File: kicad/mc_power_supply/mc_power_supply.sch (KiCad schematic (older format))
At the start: 20 parts

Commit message: Приступил к разработке блока питания ver.3 для измерительного микрофофона.
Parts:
- added C1, C2: 1 мк 275В, symbol LFcapitors:CAPITORS
- added LL1: B82731T2301A020, symbol LFtransformator:CHOKES_PL
- added R1: 500 к, symbol LFresistor:RESISTOR
- added RU1: B72210S0271K101, symbol LFresistor:VARISTOR
- added XP2: L-KLS8-01128-PC-250-0.8, ~, symbol LFconnectors:connector_1pin_gost
- C3: renamed from C1; value 470 мк 35 В -> 4700 мк 35 В; footprint (none) -> IWcomponents:CAPACITOR_10_D22
- C4: renamed from C2; value 47 мк 25 В -> 470 мк 35 В; footprint (none) -> IWcomponents:CAPACITOR_5.08_D13
- C5: renamed from C3; footprint (none) -> IWsmd_case:SMD0805
- R2: renamed from R1; footprint (none) -> IWsmd_case:SMD0805
- VD1, VD2, VD3, VD4, VD5: value MBRS1100T3G -> VS-10MQ100NTRPBF
- VD6: renamed from VD5; value GNL-3014PGC -> GNL-3014BC
- XP1: renamed from XS1; value DG126-5.0-02P-14 -> L-KLS8-01128-PC-250-0.8; symbol LFconnectors:connector_2pin_gost -> LFconnectors:connector_1pin_gost
- XP3: renamed from XP1; footprint ~ -> IWconnectors:WF-2
- XS1: renamed from XS3; value WF-3 -> Neutrik NC3FD-L1
- XS2: renamed from XS4; value WF-2 -> BNC-BJ
- renumbered R2 to R3, R3 to R4, XS2 to XS3
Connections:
- net at TV1.1: now also C2.1, LL1.3; no longer FU1.2
- net at TV1.5: now also C2.2, LL1.4; no longer XP1.2
- new net: C1.1, FU1.2, LL1.2, R1.2, RU1.1
- new net: C1.2, LL1.1, R1.1, RU1.2, XP2.1
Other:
- note added: "* Источник питания предназначен для\n питания микрофонного усилителя.\n Диапазон выходного напряжения\n от 9В до 15В при токе 0.5А"
- note removed: "* Источник питания выдаёт напряжение\n для питания микрофонного усилителя\n в диапазоне от 9В до 15В при токе 0.5А"
- moved on the sheet: C3, C4, C5, DA1, FU1, R2, R3, R4, TV1, VD1, VD2, VD3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

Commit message: Приступил к расположению компонентов на плате mc_power_supply_ver3.
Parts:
- C1, C2: footprint (none) -> IWcomponents:CAPACITOR_B32923_26.5x11
- C4: footprint IWcomponents:CAPACITOR_5.08_D13 -> IWcomponents:CAPACITOR_5.08_D10
- DA1: value LM317KTTR -> LM317D2T-TR; footprint ~ -> Package_TO:TO-263-3_TabPin2
- FU1: footprint ~ -> IWcomponents:FU_PTF15B
- LL1: footprint (none) -> IWtransformator:EMI_EPCOS_B82731T
- R1: footprint (none) -> IWsmd_case:SMD2512
- R3: footprint (none) -> IWsmd_case:BOURNS_3224W
- RU1: footprint (none) -> IWcomponents:RU_EPCOS_B72210S0271K101_12х5
- TV1: value ТПГ-112 (12В) -> ТПГ-112-12; footprint (none) -> IWtransformator:TPG112-12; symbol LFtransformator:BVEI_302_2020 -> LFtransformator:TPG-112-12
- VD1, VD2, VD3, VD4, VD5: footprint (none) -> IWcomponents:SMA
- XP1, XP2: footprint ~ -> IWconnectors:TERMINAL_KLS8-01128_6.3mm
- XS1, XS2, XS3: footprint ~ -> (none)
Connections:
- net at C2.1, LL1.3: now also TV1.5; no longer TV1.1
- net at C2.2, LL1.4: now also TV1.1; no longer TV1.5
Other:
- moved on the sheet: C1, C2, FU1, LL1, R1, RU1, XP1, XP2
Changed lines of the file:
@@
 P 8650 3750
 F 0 "DA1" H 8900 3900 60  0000 C CNN
-F 1 "LM317KTTR" H 8900 3800 60  0000 C CNN
-F 2 "~" H 8650 3750 60  0000 C CNN
+F 1 "LM317D2T-TR" H 8900 3800 60  0000 C CNN
+F 2 "Package_TO:TO-263-3_TabPin2" H 8650 3750 60  0001 C CNN
 F 3 "~" H 8650 3750 60  0000 C CNN
 	1    8650 3750
@@
 $EndComp
 $Comp
-L LFtransformator:BVEI_302_2020 TV1
+L LFtransformator:TPG-112-12 TV1
 U 1 1 55462143
 P 5850 4300
-F 0 "TV1" H 6050 4500 60  0000 C CNN
-F 1 "ТПГ-112 (12В)" H 6050 4400 60  0000 C CNN
-F 2 "" H 5850 4300 60  0001 C CNN
+F 0 "TV1" H 6050 4650 60  0000 C CNN
+F 1 "ТПГ-112-12" H 6050 4500 60  0000 C CNN
+F 2 "IWtransformator:TPG112-12" H 5850 4300 60  0001 C CNN
 F 3 "" H 5850 4300 60  0000 C CNN
 	1    5850 4300
@@
 L LFcomponents:PROTECTOR FU1
 U 1 1 5546217A
-P 3100 4200
-F 0 "FU1" H 3200 4450 60  0000 C CNN
-F 1 "0.25 A" H 3200 4350 60  0000 C CNN
-F 2 "~" H 3100 4200 60  0000 C CNN
-F 3 "~" H 3100 4200 60  0000 C CNN
-	1    3100 4200
+P 3250 4200
+F 0 "FU1" H 3350 4450 60  0000 C CNN
+F 1 "0.25 A" H 3350 4350 60  0000 C CNN
+F 2 "IWcomponents:FU_PTF15B" H 3250 4200 60  0001 C CNN
+F 3 "~" H 3250 4200 60  0000 C CNN
+	1    3250 4200
 	1    0    0    -1
 $EndComp
@@
 L LFconnectors:connector_1pin_gost XP1
 U 1 1 554621C8
-P 2750 4200
-F 0 "XP1" H 3100 4500 50  0000 L BNN
-F 1 "L-KLS8-01128-PC-250-0.8" H 2600 4400 50  0000 L BNN
-F 2 "~" H 3200 4350 50  0001 C CNN
-F 3 "" H 2750 4200 60  0000 C CNN
-	1    2750 4200
+P 2900 4200
+F 0 "XP1" H 3250 4500 50  0000 L BNN
+F 1 "L-KLS8-01128-PC-250-0.8" H 2750 4400 50  0000 L BNN
+F 2 "IWconnectors:TERMINAL_KLS8-01128_6.3mm" H 3350 4350 50  0001 C CNN
+F 3 "" H 2900 4200 60  0000 C CNN
+	1    2900 4200
 	-1   0    0    -1
 $EndComp
 Wire Wire Line
-	2750 4200 3100 4200
+	2900 4200 3250 4200
 $Comp
 L LFdiod:SHOTTKY_DIODE VD1
@@
 F 0 "VD1" H 7100 4200 71  0000 C CNN
 F 1 "VS-10MQ100NTRPBF" H 7250 4050 71  0000 C CNN
-F 2 "" H 6750 4300 60  0001 C CNN
+F 2 "IWcomponents:SMA" H 6750 4300 60  0001 C CNN
 F 3 "" H 6750 4300 60  0000 C CNN
 	1    6750 4300
@@
 F 0 "VD4" H 7900 4750 71  0000 C CNN
 F 1 "VS-10MQ100NTRPBF" H 7800 4650 71  0000 C CNN
-F 2 "" H 7750 4300 60  0001 C CNN
+F 2 "IWcomponents:SMA" H 7750 4300 60  0001 C CNN
 F 3 "" H 7750 4300 60  0000 C CNN
 	1    7750 4300
@@
 F 0 "VD2" H 7200 4400 71  0000 C CNN
 F 1 "VS-10MQ100NTRPBF" H 7350 4250 71  0000 C CNN
-F 2 "" H 7050 4750 60  0001 C CNN
+F 2 "IWcomponents:SMA" H 7050 4750 60  0001 C CNN
 F 3 "" H 7050 4750 60  0000 C CNN
 	1    7050 4750
@@
 F 0 "VD3" H 7600 4400 71  0000 C CNN
 F 1 "VS-10MQ100NTRPBF" H 7950 4250 71  0000 C CNN
-F 2 "" H 7450 4750 60  0001 C CNN
+F 2 "IWcomponents:SMA" H 7450 4750 60  0001 C CNN
 F 3 "" H 7450 4750 60  0000 C CNN
 	1    7450 4750
@@
 F 0 "R3" V 9600 4450 71  0000 C CNN
 F 1 "5 к" V 9700 4450 71  0000 C CNN
-F 2 "" H 9500 4650 60  0001 C CNN
+F 2 "IWsmd_case:BOURNS_3224W" H 9500 4650 60  0001 C CNN
 F 3 "" H 9500 4650 60  0000 C CNN
 	1    9500 4650
@@
 F 0 "XS1" H 12450 4900 50  0000 L BNN
 F 1 "Neutrik NC3FD-L1" H 12250 4800 50  0000 L BNN
-F 2 "~" H 12650 4750 50  0001 C CNN
+F 2 "" H 12650 4750 50  0001 C CNN
 F 3 "" H 12200 4600 60  0000 C CNN
 	1    12200 4600
@@
 F 0 "XS2" H 12500 5850 50  0000 L BNN
 F 1 "BNC-BJ " H 12400 5750 50  0000 L BNN
-F 2 "~" H 12700 5700 50  0001 C CNN
+F 2 "" H 12700 5700 50  0001 C CNN
 F 3 "" H 12250 5550 60  0000 C CNN
 	1    12250 5550
@@
 F 0 "VD5" H 9250 3700 71  0000 C CNN
 F 1 "VS-10MQ100NTRPBF" H 9250 3600 71  0000 C CNN
-F 2 "" H 9100 3450 60  0001 C CNN
+F 2 "IWcomponents:SMA" H 9100 3450 60  0001 C CNN
 F 3 "" H 9100 3450 60  0000 C CNN
 	1    9100 3450
@@
 Text Notes 12635 4640 0    50   ~ 0
 GND
-Text Notes 2020 4240 0    50   ~ 0
+Text Notes 2170 4240 0    50   ~ 0
 220В 50Гц
 Text Notes 2250 7050 0    60   ~ 0
@@
 F 0 "C4" H 10450 4550 71  0000 C CNN
 F 1 "470 мк 35 В" H 10450 4450 71  0000 C CNN
-F 2 "IWcomponents:CAPACITOR_5.08_D13" H 10250 4250 60  0001 C CNN
+F 2 "IWcomponents:CAPACITOR_5.08_D10" H 10250 4250 60  0001 C CNN
 F 3 "" H 10250 4250 60  0000 C CNN
 	1    10250 4250
@@
 F 0 "XS3" H 13300 4300 50  0000 L BNN
 F 1 "HU-2" H 13250 4200 50  0000 L BNN
-F 2 "~" H 13400 4150 50  0001 C CNN
+F 2 "" H 13400 4150 50  0001 C CNN
 F 3 "" H 12950 4000 60  0000 C CNN
 	1    12950 4000
@@
 L LFconnectors:connector_1pin_gost XP2
 U 1 1 60118508
-P 2750 4700
-F 0 "XP2" H 3100 5000 50  0000 L BNN
-F 1 "L-KLS8-01128-PC-250-0.8" H 2600 4900 50  0000 L BNN
-F 2 "~" H 3200 4850 50  0001 C CNN
-F 3 "" H 2750 4700 60  0000 C CNN
-	1    2750 4700
+P 2900 4700
+F 0 "XP2" H 3250 5000 50  0000 L BNN
+F 1 "L-KLS8-01128-PC-250-0.8" H 2750 4900 50  0000 L BNN
+F 2 "IWconnectors:TERMINAL_KLS8-01128_6.3mm" H 3350 4850 50  0001 C CNN
+F 3 "" H 2900 4700 60  0000 C CNN
+	1    2900 4700
 	-1   0    0    -1
 $EndComp
-Text Notes 2020 4740 0    50   ~ 0
+Text Notes 2170 4740 0    50   ~ 0
 220В 50Гц
 $Comp
 L LFcapitors:CAPITORS C1
 U 1 1 60135059
-P 4300 4350
-F 0 "C1" V 4750 4350 71  0000 C CNN
-F 1 "1 мк 275В" V 4900 4350 71  0000 C CNN
-F 2 "" H 4300 4350 60  0001 C CNN
-F 3 "" H 4300 4350 60  0000 C CNN
-	1    4300 4350
+P 4450 4350
+F 0 "C1" V 4900 4350 71  0000 C CNN
+F 1 "1 мк 275В" V 5050 4350 71  0000 C CNN
+F 2 "IWcomponents:CAPACITOR_B32923_26.5x11" H 4450 4350 60  0001 C CNN
+F 3 "" H 4450 4350 60  0000 C CNN
+	1    4450 4350
 	0    1    1    0
 $EndComp
 Wire Wire Line
-	3350 4200 3650 4200
-Wire Wire Line
-	4300 4600 4300 4700
-Wire Wire Line
-	2750 4700 3650 4700
+	3500 4200 3800 4200
+Wire Wire Line
+	4450 4600 4450 4700
+Wire Wire Line
+	2900 4700 3800 4700
 $Comp
 L LFtransformator:CHOKES_PL LL1
 U 1 1 60142715
-P 5200 4350
-F 0 "LL1" V 4953 4050 60  0000 C CNN
-F 1 "B82731T2301A020" V 5059 4050 60  0000 C CNN
-F 2 "" H 5200 4350 60  0001 C CNN
-F 3 "" H 5200 4350 60  0000 C CNN
-	1    5200 4350
+P 5350 4350
+F 0 "LL1" V 5103 4050 60  0000 C CNN
+F 1 "B82731T2301A020" V 5209 4050 60  0000 C CNN
+F 2 "IWtransformator:EMI_EPCOS_B82731T" H 5350 4350 60  0001 C CNN
+F 3 "" H 5350 4350 60  0000 C CNN
+	1    5350 4350
 	0    1    1    0
 $EndComp
 Wire Wire Line
-	4600 4350 4450 4350
-Wire Wire Line
-	4450 4200 4300 4200
-Connection ~ 4300 4200
-Wire Wire Line
-	4300 4700 4450 4700
-Wire Wire Line
-	4450 4700 4450 4550
-Wire Wire Line
-	4450 4550 4600 4550
-Connection ~ 4300 4700
-Wire Wire Line
-	5200 4350 5350 4350
-Wire Wire Line
-	5350 4350 5350 4200
-Wire Wire Line
-	5350 4200 5500 4200
-Wire Wire Line
-	5200 4550 5350 4550
-Wire Wire Line
-	5350 4550 5350 4700
-Wire Wire Line
-	5350 4700 5500 4700
+	4750 4350 4600 4350
+Wire Wire Line
+	4600 4200 4450 4200
+Connection ~ 4450 4200
+Wire Wire Line
+	4450 4700 4600 4700
+Wire Wire Line
+	4600 4700 4600 4550
+Wire Wire Line
+	4600 4550 4750 4550
+Connection ~ 4450 4700
+Wire Wire Line
+	5350 4350 5500 4350
+Wire Wire Line
+	5500 4350 5500 4200
+Wire Wire Line
+	5500 4200 5700 4200
+Wire Wire Line
+	5350 4550 5500 4550
+Wire Wire Line
+	5500 4550 5500 4700
+Wire Wire Line
+	5500 4700 5700 4700
 $Comp
 L LFresistor:RESISTOR R1
 U 1 1 6015F13E
-P 4000 4600
-F 0 "R1" V 4650 4600 71  0000 C CNN
-F 1 "500 к" V 4500 4600 71  0000 C CNN
-F 2 "" H 4000 4600 60  0001 C CNN
-F 3 "" H 4000 4600 60  0000 C CNN
-	1    4000 4600
+P 4150 4600
+F 0 "R1" V 4800 4600 71  0000 C CNN
+F 1 "500 к" V 4650 4600 71  0000 C CNN
+F 2 "IWsmd_case:SMD2512" H 4150 4600 60  0001 C CNN
+F 3 "" H 4150 4600 60  0000 C CNN
+	1    4150 4600
 	0    -1   -1   0
 $EndComp
-Connection ~ 4000 4200
-Wire Wire Line
-	4000 4200 4300 4200
-Wire Wire Line
-	4000 4600 4000 4700
-Connection ~ 4000 4700
-Wire Wire Line
-	4000 4700 4300 4700
+Connection ~ 4150 4200
+Wire Wire Line
+	4150 4200 4450 4200
+Wire Wire Line
+	4150 4600 4150 4700
+Connection ~ 4150 4700
+Wire Wire Line
+	4150 4700 4450 4700
 $Comp
 L LFresistor:VARISTOR RU1
 U 1 1 6016D315
-P 3650 4350
-F 0 "RU1" V 3900 3950 71  0000 L CNN
-F 1 "B72210S0271K101" V 4100 3550 71  0000 L CNN
-F 2 "" H 3650 4350 60  0001 C CNN
-F 3 "~" V 3856 4477 60  0000 L CNN
-	1    3650 4350
+P 3800 4350
+F 0 "RU1" V 4050 3950 71  0000 L CNN
+F 1 "B72210S0271K101" V 4250 3550 71  0000 L CNN
+F 2 "IWcomponents:RU_EPCOS_B72210S0271K101_12х5" H 3800 4350 60  0001 C CNN
+F 3 "~" V 4006 4477 60  0000 L CNN
+	1    3800 4350
 	0    1    1    0
 $EndComp
 Wire Wire Line
+	4600 4200 4600 4350
+Wire Wire Line
 	4450 4200 4450 4350
 Wire Wire Line
-	4300 4200 4300 4350
-Wire Wire Line
-	4000 4200 4000 4350
-Wire Wire Line
-	3650 4350 3650 4200
-Connection ~ 3650 4200
-Wire Wire Line
-	3650 4200 4000 4200
-Wire Wire Line
-	3650 4600 3650 4700
-Connection ~ 3650 4700
-Wire Wire Line
-	3650 4700 4000 4700
-Wire Wire Line
-	5500 4200 5500 4350
-Wire Wire Line
-	5500 4600 5500 4700
+	4150 4200 4150 4350
+Wire Wire Line
+	3800 4350 3800 4200
+Connection ~ 3800 4200
+Wire Wire Line
+	3800 4200 4150 4200
+Wire Wire Line
+	3800 4600 3800 4700
+Connection ~ 3800 4700
+Wire Wire Line
+	3800 4700 4150 4700
+Wire Wire Line
+	5700 4200 5700 4350
+Wire Wire Line
+	5700 4600 5700 4700
 $Comp
 L LFcapitors:CAPITORS C2
 U 1 1 60146CF7
-P 5500 4350
-F 0 "C2" V 5950 4350 71  0000 C CNN
-F 1 "1 мк 275В" V 6100 4350 71  0000 C CNN
-F 2 "" H 5500 4350 60  0001 C CNN
-F 3 "" H 5500 4350 60  0000 C CNN
-	1    5500 4350
+P 5700 4350
+F 0 "C2" V 6150 4350 71  0000 C CNN
+F 1 "1 мк 275В" V 6300 4350 71  0000 C CNN
+F 2 "IWcomponents:CAPACITOR_B32923_26.5x11" H 5700 4350 60  0001 C CNN
+F 3 "" H 5700 4350 60  0000 C CNN
+	1    5700 4350
 	0    1    1    0
 $EndComp
-Wire Wire Line
-	5850 4300 5650 4300
-Wire Wire Line
-	5650 4300 5650 4200
-Wire Wire Line
-	5650 4200 5500 4200
-Connection ~ 5500 4200
-Wire Wire Line
-	5850 4600 5650 4600
-Wire Wire Line
-	5650 4600 5650 4700
-Wire Wire Line
-	5650 4700 5500 4700
-Connection ~ 5500 4700
+Connection ~ 5700 4200
+Connection ~ 5700 4700
 Wire Wire Line
 	12900 6250 13150 6250
@@
 	1    0    0    -1
 $EndComp
+Wire Wire Line
+	5700 4200 5850 4200
+Wire Wire Line
+	5700 4700 5850 4700
 $EndSCHEMATC

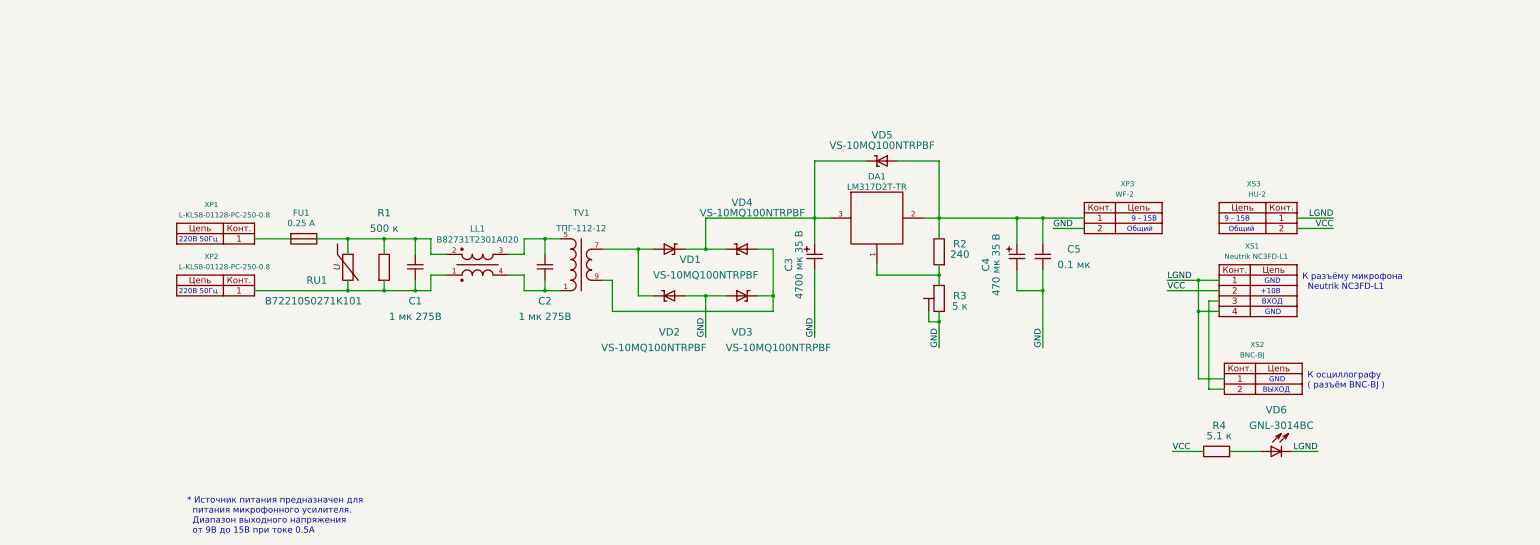
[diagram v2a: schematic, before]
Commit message: Заменил трансформатор на плате MM power supply ver. 3.0. и приступил к повторной трассировке.
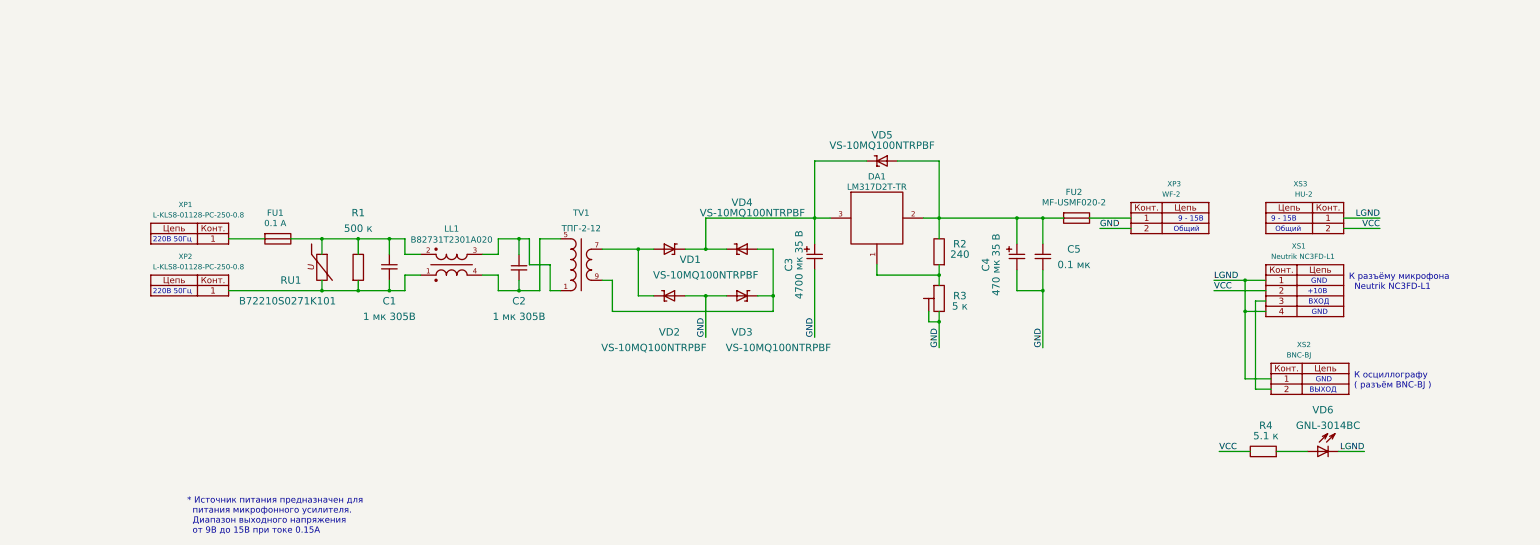
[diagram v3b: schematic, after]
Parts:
- added FU2: MF-USMF020-2, IWsmd_case:SMD1210, symbol LFcomponents:PROTECTOR
- C1, C2: value 1 мк 275В -> 1 мк 305В
- FU1: value 0.25 A -> 0.1 A
- TV1: value ТПГ-112-12 -> ТПГ-2-12; footprint IWtransformator:TPG112-12 -> IWtransformator:TPG2-12
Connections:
- net at C4.1, C5.1, DA1.2 (Vout)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: now also FU2.1; no longer XP3.1
- net at C2.2, TV1.1: now also LL1.3; no longer LL1.4
- net at C2.1, TV1.5: now also LL1.4; no longer LL1.3
- new net: FU2.2, XP3.1
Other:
- note added: "* Источник питания предназначен для\n питания микрофонного усилителя.\n Диапазон выходного напряжения\n от 9В до 15В при токе 0.15А"
- note removed: "* Источник питания предназначен для\n питания микрофонного усилителя.\n Диапазон выходного напряжения\n от 9В до 15В при токе 0.5А"
- moved on the sheet: C1, C2, FU1, LL1, R1, R4, RU1, VD6, XP1, XP2, XP3, XS1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

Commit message: Повторно произвёл трассировку платы mc_power_supply_ver_3.0.
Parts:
- R1: value 500 к -> 510 к
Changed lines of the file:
@@
 P 3900 4600
 F 0 "R1" V 4550 4600 71  0000 C CNN
-F 1 "500 к" V 4400 4600 71  0000 C CNN
+F 1 "510 к" V 4400 4600 71  0000 C CNN
 F 2 "IWsmd_case:SMD2512" H 3900 4600 60  0001 C CNN
 F 3 "" H 3900 4600 60  0000 C CNN

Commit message: Поправил трассировку на платы mc_power_supply_ver_3.0.
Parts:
- DA1: footprint Package_TO:TO-263-3_TabPin2 -> IWsmd_case:TO-252-3_TabPin_2
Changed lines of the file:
@@
 F 0 "DA1" H 8900 3900 60  0000 C CNN
 F 1 "LM317D2T-TR" H 8900 3800 60  0000 C CNN
-F 2 "Package_TO:TO-263-3_TabPin2" H 8650 3750 60  0001 C CNN
+F 2 "IWsmd_case:TO-252-3_TabPin_2" H 8650 3750 60  0001 C CNN
 F 3 "~" H 8650 3750 60  0000 C CNN
 	1    8650 3750

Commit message: Поравил плату mc_power_supply ver.3.
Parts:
- DA1: footprint IWsmd_case:TO-252-3_TabPin_2 -> IWsmd_case:TO-263-3_TabPin_2
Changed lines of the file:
@@
 F 0 "DA1" H 8900 3900 60  0000 C CNN
 F 1 "LM317D2T-TR" H 8900 3800 60  0000 C CNN
-F 2 "IWsmd_case:TO-252-3_TabPin_2" H 8650 3750 60  0001 C CNN
+F 2 "IWsmd_case:TO-263-3_TabPin_2" H 8650 3750 60  0001 C CNN
 F 3 "~" H 8650 3750 60  0000 C CNN
 	1    8650 3750

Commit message: Продолжил разрабатывать плату mc_power_supply.
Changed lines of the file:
@@
 U 1 1 6015F13E
 P 3900 4600
-F 0 "R1" V 4550 4600 71  0000 C CNN
+F 0 "R1" V 4550 4650 71  0000 C CNN
 F 1 "510 к" V 4400 4600 71  0000 C CNN
 F 2 "IWsmd_case:SMD2512" H 3900 4600 60  0001 C CNN
@@
 U 1 1 6016D315
 P 3550 4350
-F 0 "RU1" V 3800 3950 71  0000 L CNN
-F 1 "B72210S0271K101" V 4000 3550 71  0000 L CNN
+F 0 "RU1" V 4000 4200 71  0000 L CNN
+F 1 "B72210S0271K101" V 4150 3400 71  0000 L CNN
 F 2 "IWcomponents:RU_EPCOS_B72210S0271K101_12х5" H 3550 4350 60  0001 C CNN
 F 3 "~" V 3756 4477 60  0000 L CNN

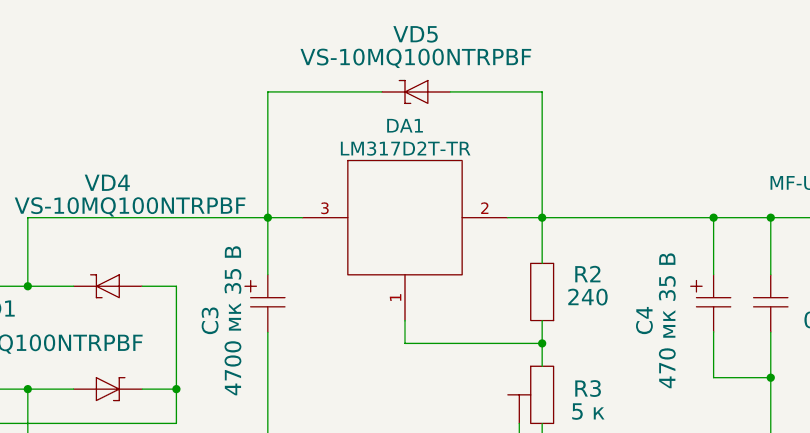
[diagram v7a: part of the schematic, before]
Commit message: Успешно изготовил и проверил первый экземляр платы MM_power_supply_ver. 3.0
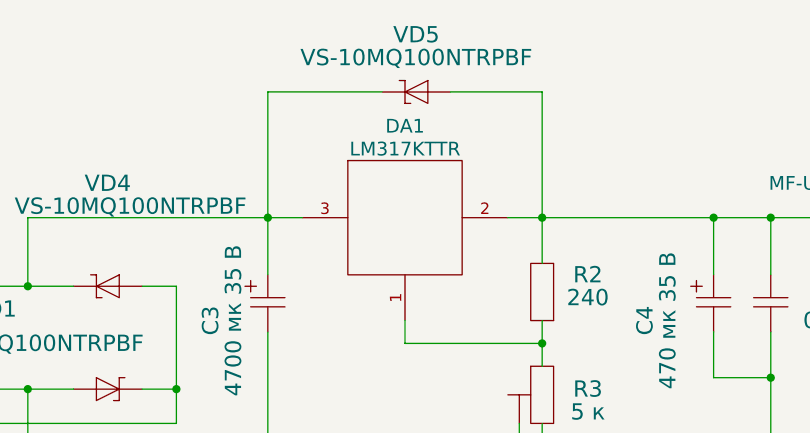
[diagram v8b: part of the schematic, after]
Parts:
- DA1: value LM317D2T-TR -> LM317KTTR
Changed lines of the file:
@@
 P 8650 3750
 F 0 "DA1" H 8900 3900 60  0000 C CNN
-F 1 "LM317D2T-TR" H 8900 3800 60  0000 C CNN
+F 1 "LM317KTTR" H 8900 3800 60  0000 C CNN
 F 2 "IWsmd_case:TO-263-3_TabPin_2" H 8650 3750 60  0001 C CNN
 F 3 "~" H 8650 3750 60  0000 C CNN
